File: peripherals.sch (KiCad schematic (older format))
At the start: 36 parts, among them J10 PIO Header, J6 CT0, J7 Port A, J8 Port A, J9 IDE, U11 Z84C3010AEG, U12 Z84C4310AEG, U13 Z84C2010AEG

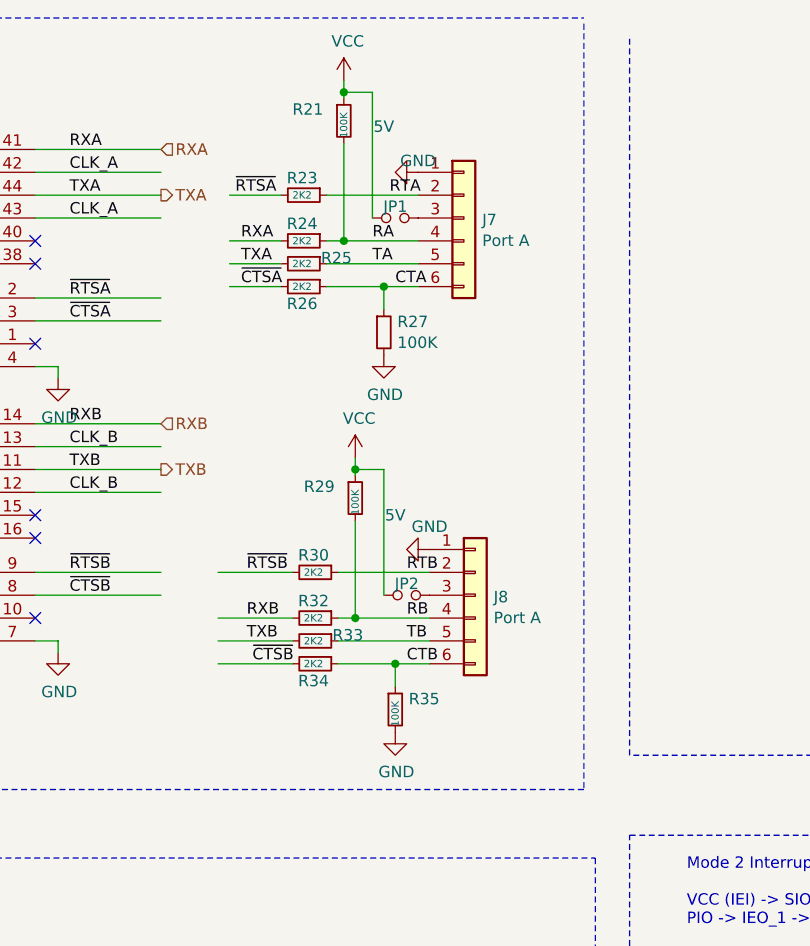
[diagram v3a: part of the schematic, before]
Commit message: Changed to resistor arrays, flipped to front-side
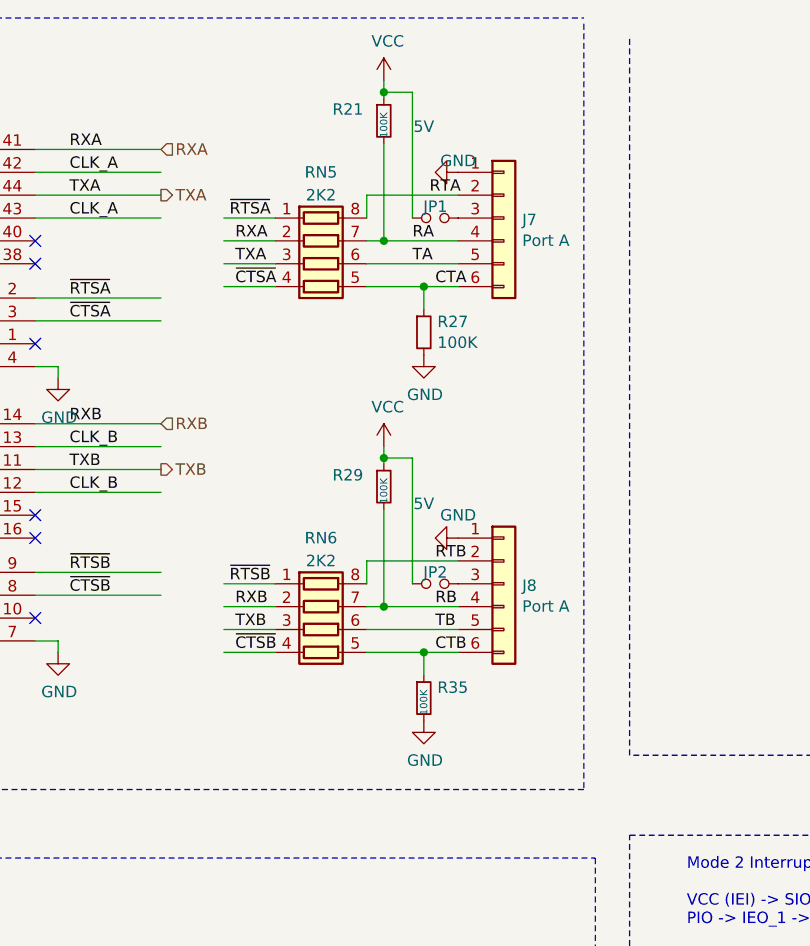
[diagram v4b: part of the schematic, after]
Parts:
- removed R23, R24, R25, R26, R30, R32, R33, R34: 2K2, Resistor_SMD:R_0603_1608Metric_Pad1.05x0.95mm_HandSolder, symbol THS-80-rescue:R_Small-Device-sbc_z80-rescue
- added RN5, RN6: 2K2, Resistor_SMD:R_Cat16-4, symbol Device:R_Pack04
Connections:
- wire segments 201 -> 203
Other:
- moved on the sheet: J7, J8, JP1, JP2, R21, R27, R29, R35

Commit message: fixed clocks
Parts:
- removed J6: CT0, Connector_PinHeader_2.54mm:PinHeader_1x03_P2.54mm_Horizontal, symbol Connector_Generic:Conn_01x03
- removed R22, R28, R36: 10K, Resistor_SMD:R_0603_1608Metric_Pad1.05x0.95mm_HandSolder, symbol Device:R_Small
- renumbered C29 to C20, C30 to C21, C31 to C22, C28 to C23, D16 to D10, J10 to J5, J7 to J6, J8 to J7, J9 to J8, JP1 to JP2, JP2 to JP3, JP3 to JP4, R29 to R10, R27 to R11, R35 to R12, R40 to R13, R37 to R14, R38 to R15, R39 to R16, R31 to R8, R21 to R9, U13 to U6, U12 to U7, U11 to U8
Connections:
- net labels added: ~IORD, ~IOWR, ~RM1
- net labels removed: CLK_UART, CT0, CT3, ~RESET, ~WR
- wire segments 203 -> 200
- no-connect marks 21 -> 19
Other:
- moved on the sheet: C20, C21, C22, J5, U6

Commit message: do over with additional pmod
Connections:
- net labels added: +5V
- wire segments 200 -> 207
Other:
- moved on the sheet: J6, J7, JP2, JP3, R10, R11, R12, R9, RN5, RN6
